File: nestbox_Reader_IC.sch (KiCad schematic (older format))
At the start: 46 parts, among them U2 CR95HF, Y2 ABM11-142-27.120MHz

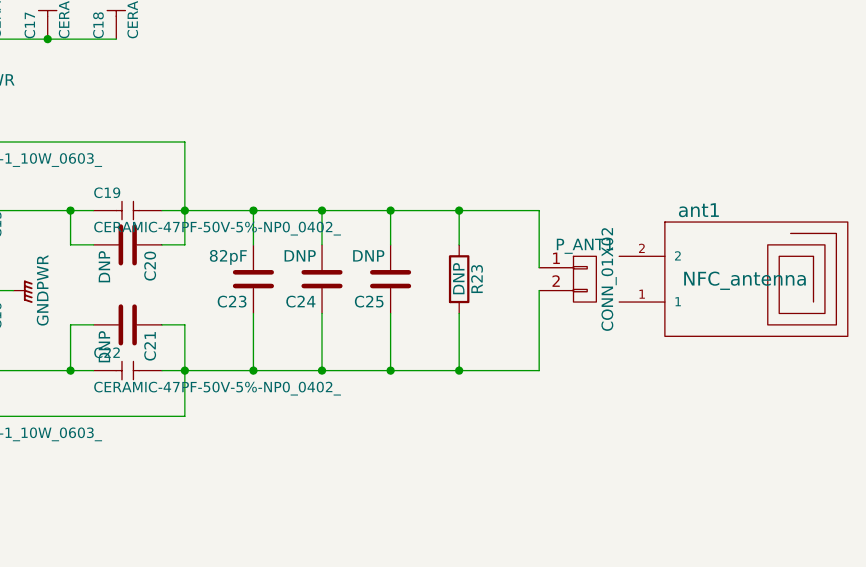
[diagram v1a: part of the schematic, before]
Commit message: circular NFC antenna added to pcb file, as well as other important changes and additions of library components
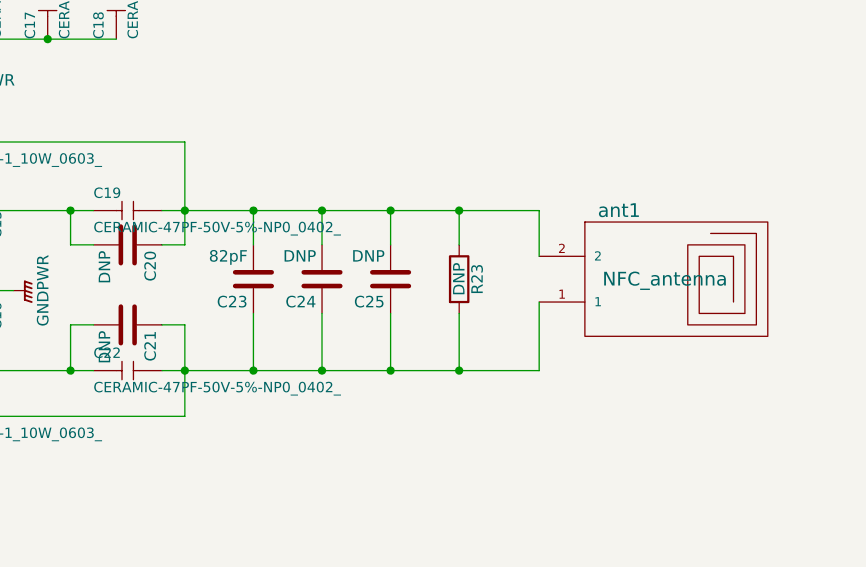
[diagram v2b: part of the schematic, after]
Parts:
- removed P_ANT1: CONN_01X02, Pin_Headers:Pin_Header_Angled_1x02, symbol CONN_01X02
- ant1: footprint (none) -> Octanis3:NFC_ANTENNA_CIRC
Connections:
- net at C19.2, C20.1, C23.2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: now also ant1.2
- net at C21.1, C22.2, C23.1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: now also ant1.1
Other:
- moved on the sheet: ant1
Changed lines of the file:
@@
 LIBS:contrib
 LIBS:valves
+LIBS:octanis3
 LIBS:SeeedOPL-Capacitor-2016
 LIBS:SeeedOPL-Connector-2016
@@
 	8250 4200 8250 4600
 Wire Wire Line
-	9800 4400 8150 4400
+	8150 4400 9800 4400
 Wire Wire Line
 	8150 4200 8250 4200
@@
 L NFC_antenna ant1
 U 1 1 587564A8
-P 10700 4000
-F 0 "ant1" H 10500 4300 60  0000 C CNN
-F 1 "NFC_antenna" H 10700 4000 60  0000 C CNN
-F 2 "" H 10700 4000 60  0001 C CNN
-F 3 "" H 10700 4000 60  0001 C CNN
-	1    10700 4000
-	1    0    0    -1
-$EndComp
-Wire Wire Line
-	9800 3700 9800 3950
+P 10350 4000
+F 0 "ant1" H 10150 4300 60  0000 C CNN
+F 1 "NFC_antenna" H 10350 4000 60  0000 C CNN
+F 2 "Octanis3:NFC_ANTENNA_CIRC" H 10350 4000 60  0001 C CNN
+F 3 "" H 10350 4000 60  0001 C CNN
+	1    10350 4000
+	1    0    0    -1
+$EndComp
+Wire Wire Line
+	9800 3700 9800 3900
 Connection ~ 9450 3700
 Wire Wire Line
-	9800 4050 9800 4400
+	9800 4400 9800 4100
 Connection ~ 9450 4400
 $Comp
@@
 Wire Wire Line
 	7200 1650 7200 1800
-$Comp
-L CONN_01X02 P_ANT1
-U 1 1 587D3970
-P 10000 4000
-F 0 "P_ANT1" H 10000 4150 50  0000 C CNN
-F 1 "CONN_01X02" V 10100 4000 50  0000 C CNN
-F 2 "Pin_Headers:Pin_Header_Angled_1x02" H 10000 4000 50  0001 C CNN
-F 3 "" H 10000 4000 50  0000 C CNN
-	1    10000 4000
-	1    0    0    -1
-$EndComp
 $EndSCHEMATC

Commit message: updated schematics and BOM with MPN
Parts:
- C23: MPN (none) -> GQM1875C2E820JB12D
- FI1: MPN (none) -> NFM18PS105R0J3D
- L2, L5: MPN (none) -> 742792042
- L3, L4: MPN (none) -> CV201210-R56K
- L6: MPN (none) -> 742792093
- U2: value CR95HF -> ST95HF; MPN (none) -> ST95HF-VMD5T
- Y2: MPN (none) -> ABM11-142-27.120MHz-T3
